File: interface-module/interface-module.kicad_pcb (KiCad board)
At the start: 2 copper layers, 79 x 83 mm, 113 parts, among them J1 Conn_01x08, J2 Conn_01x08, J3 Conn_01x02, Q201 DMP3050LVT-7, Q202 DMP3050LVT-7, Q203 DMP3050LVT-7, Q204 DMP3050LVT-7, Q205 DMP3050LVT-7, Q206 DMP3050LVT-7, Q207 DMP3050LVT-7, Q208 DMP3050LVT-7, SW1 SW_Coded_SH-7050, U101 MCP3464, U201 140357145200, U202 140357145200, U203 140357145200, U204 140357145200, U205 140357145200, U206 140357145200, U207 140357145200, U208 140357145200, U301 TCA9548

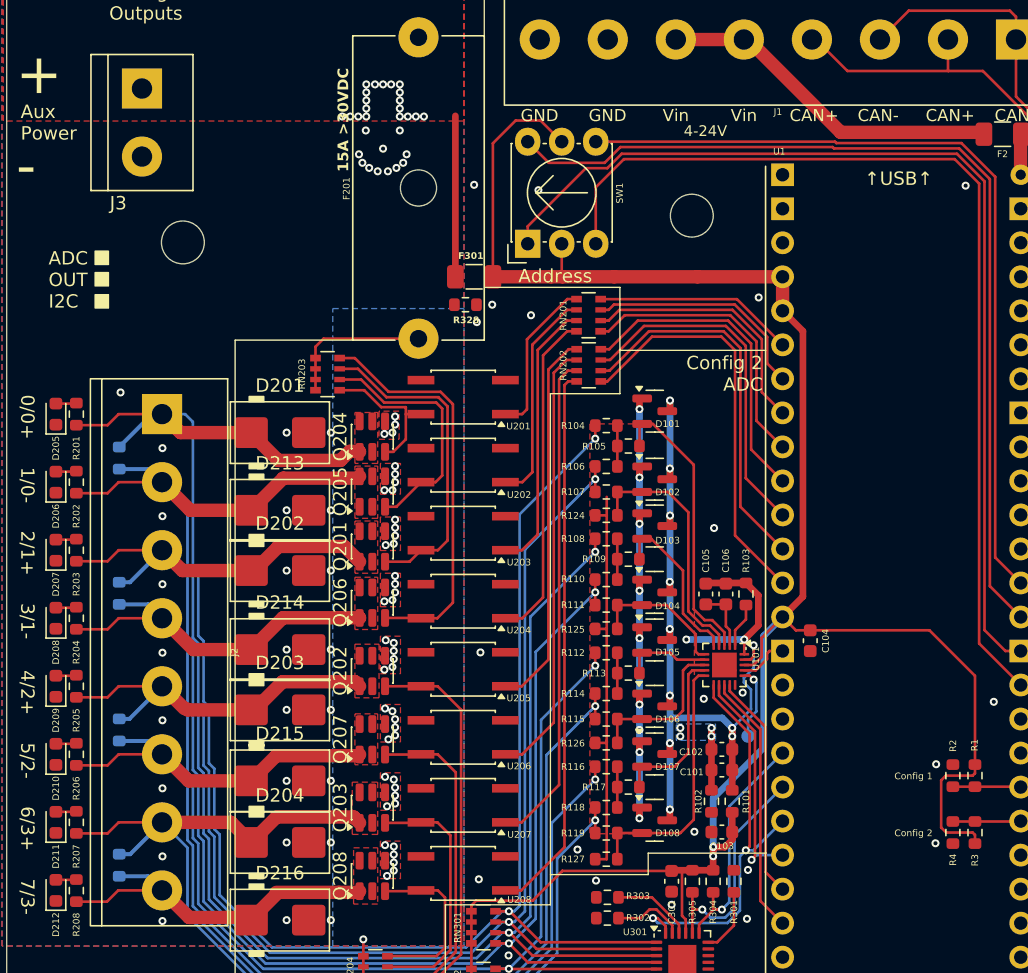
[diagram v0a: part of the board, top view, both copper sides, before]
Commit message: Clean up DRC violations
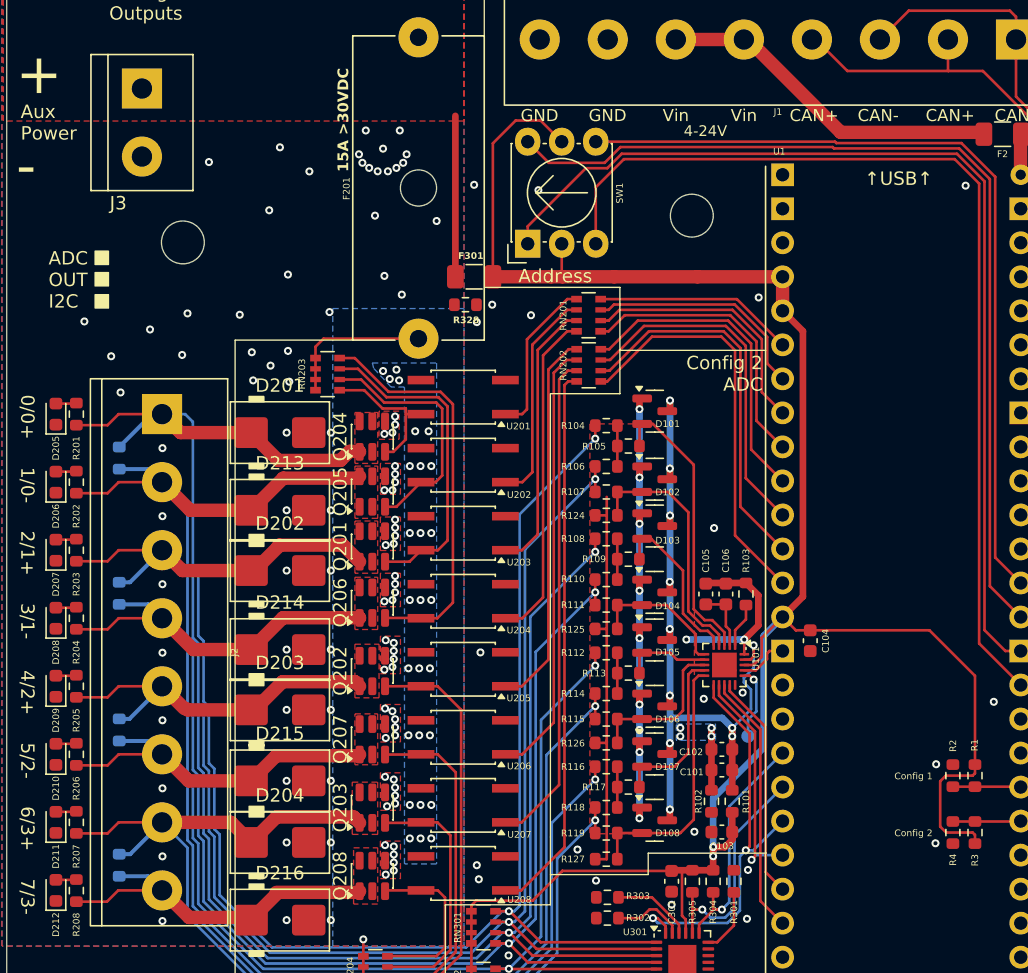
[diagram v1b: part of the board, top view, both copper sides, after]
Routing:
- net GND: vias 32 -> 33
- net AUX_POW-: vias 36 -> 84
- net AUX_POW+: vias 19 -> 0

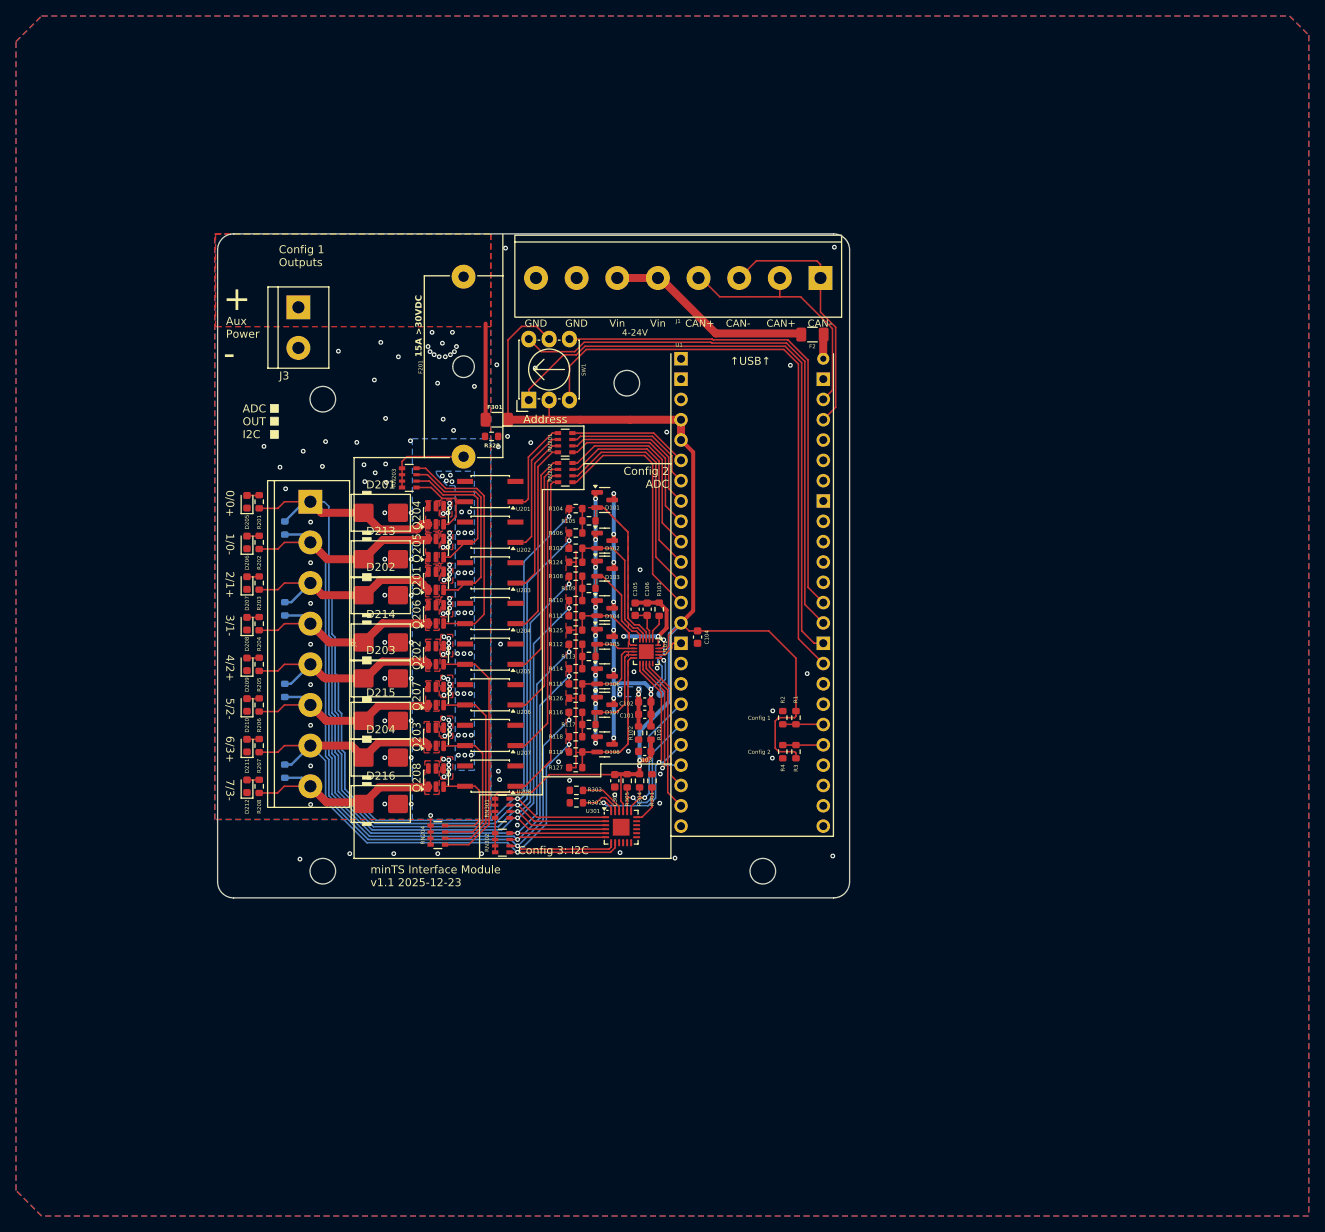
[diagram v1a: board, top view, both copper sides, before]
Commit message: Final polish before manufacturing (v1.1)
Upped version to 1.1. Cleared ERC errors, one interesting one left that won't stop manufacturing. Cleared all DRC warnings and
errors. Formatted BOM. Fixed BOM for important parts. Added fuse parts for reference. Cleaned up silkscreen.
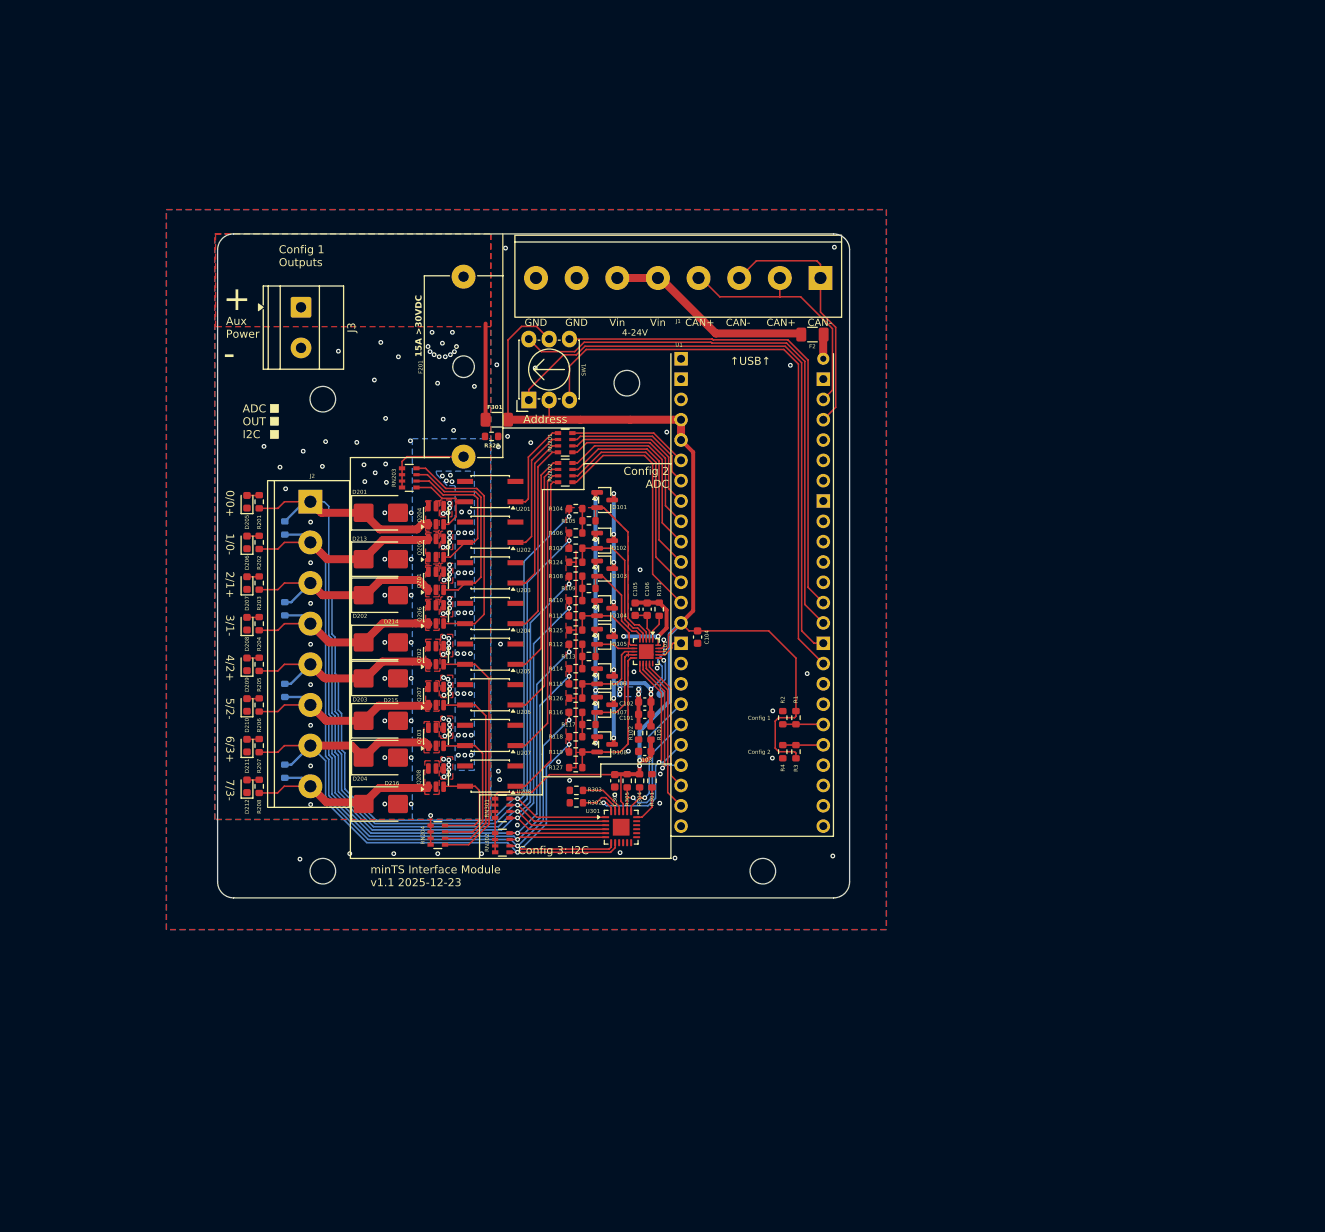
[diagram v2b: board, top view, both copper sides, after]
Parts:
- D201, D202, D203, D204, D213, D214, D215, D216: value SMBJ5.0A -> SMBJ5360B-TP; footprint PCM_Diode_SMD_AKL:D_SMB -> Diode_SMD:D_SMB
- J3: footprint TerminalBlock:TerminalBlock_bornier-2_P5.08mm -> TerminalBlock_Phoenix:TerminalBlock_Phoenix_MKDS-1,5-2-5.08_1x02_P5.08mm_Horizontal
- moved J3 0.33 mm to (111.8, 72.2)

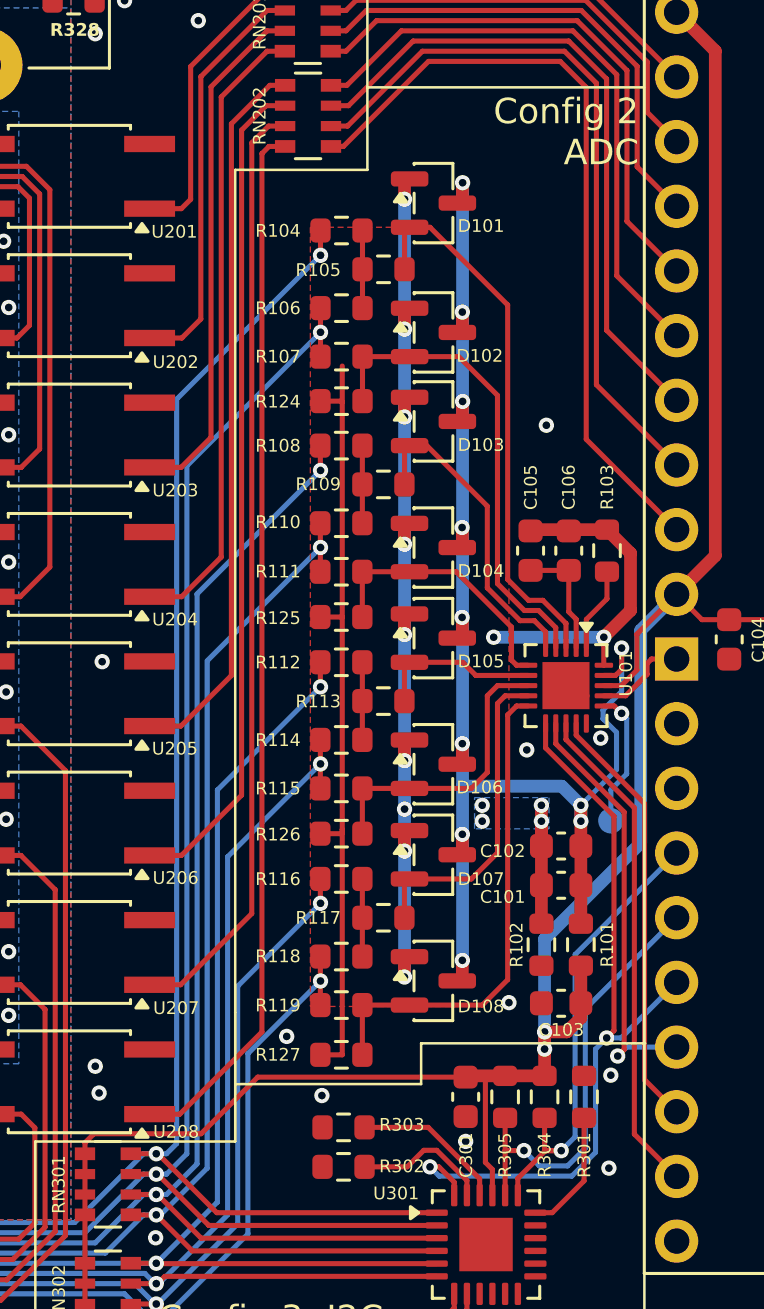
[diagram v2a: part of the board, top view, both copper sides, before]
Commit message: Fix 1SS396 pins to match datasheet w/ a new symbol/footprint
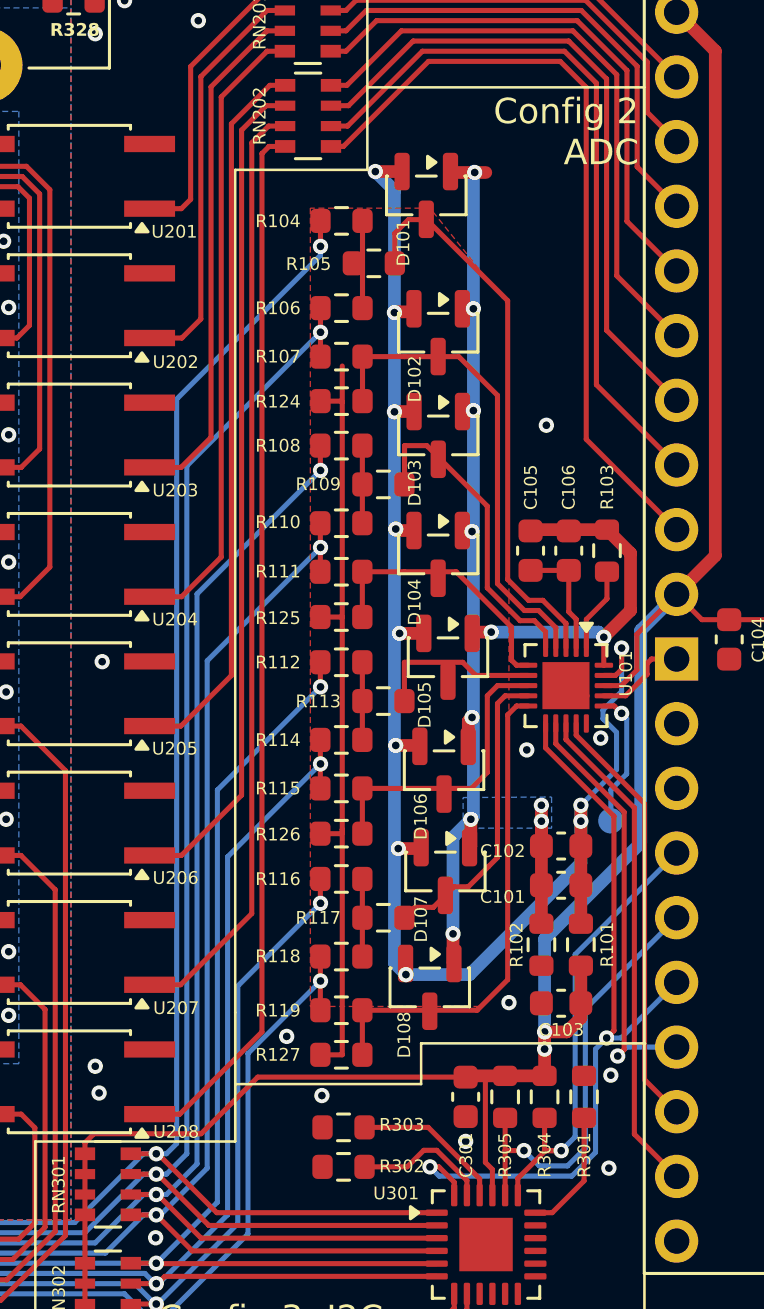
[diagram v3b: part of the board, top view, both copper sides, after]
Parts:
- F201: value 15A slow -> 5x20 mm Fuse Holder
- U101: value MCP3464 -> MCP3464R
- moved D105 0.95 mm to (150.4, 114.1), turned to -90 degrees
- moved D107 0.81 mm to (150.2, 122.5), turned to -90 degrees
- moved D103 0.58 mm to (150.0, 105.4), turned to -90 degrees
- moved D106 0.48 mm to (150.2, 118.6), turned to -90 degrees
- moved R105 0.45 mm to (147.4, 98.7)
- moved D101 0.41 mm to (149.5, 96.0), turned to -90 degrees
- moved R104 0.38 mm to (146.2, 97.0)
- moved D104 0.33 mm to (150.0, 110.1), turned to -90 degrees
- moved D108 0.29 mm to (149.6, 127.1), turned to -90 degrees
- moved R119 0.20 mm to (146.2, 128.0)
- moved D102 0.18 mm to (150.0, 101.4), turned to -90 degrees
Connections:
- D101 pad 2: IN0+ -> +3.3VA
- D101 pad 3: +3.3VA -> IN0+
- D102 pad 2: IN0- -> +3.3VA
- D102 pad 3: +3.3VA -> IN0-
- D103 pad 2: IN1+ -> +3.3VA
- D103 pad 3: +3.3VA -> IN1+
- D104 pad 2: IN1- -> +3.3VA
- D104 pad 3: +3.3VA -> IN1-
- D105 pad 2: IN2+ -> +3.3VA
- D105 pad 3: +3.3VA -> IN2+
- D106 pad 2: IN2- -> +3.3VA
- D106 pad 3: +3.3VA -> IN2-
- D107 pad 2: IN3+ -> +3.3VA
- D107 pad 3: +3.3VA -> IN3+
- D108 pad 2: IN3- -> +3.3VA
- D108 pad 3: +3.3VA -> IN3-
- U1 pad 15: GND -> +3V3
- U101 pad 17: GND -> +3V3
- U101 pad 21: GND -> +3V3
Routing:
- net +3.3VA: track 56.2 -> 63.3 mm
- net GND: track 4.71 -> 0.00 mm
- net +3V3: track 165.2 -> 169.9 mm
- net IN3+: track 12.8 -> 12.0 mm
- net GNDA: track 86.7 -> 87.2 mm, vias 15 -> 11
